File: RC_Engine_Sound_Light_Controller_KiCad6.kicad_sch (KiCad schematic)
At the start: 44 parts, among them J1 RX, J10 RGB, J11 32, J12 CH1, J13 CH2, J14 CH3, J15 ESC, J16 CH4, J17 Brushed Motor output, J2 HeadL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

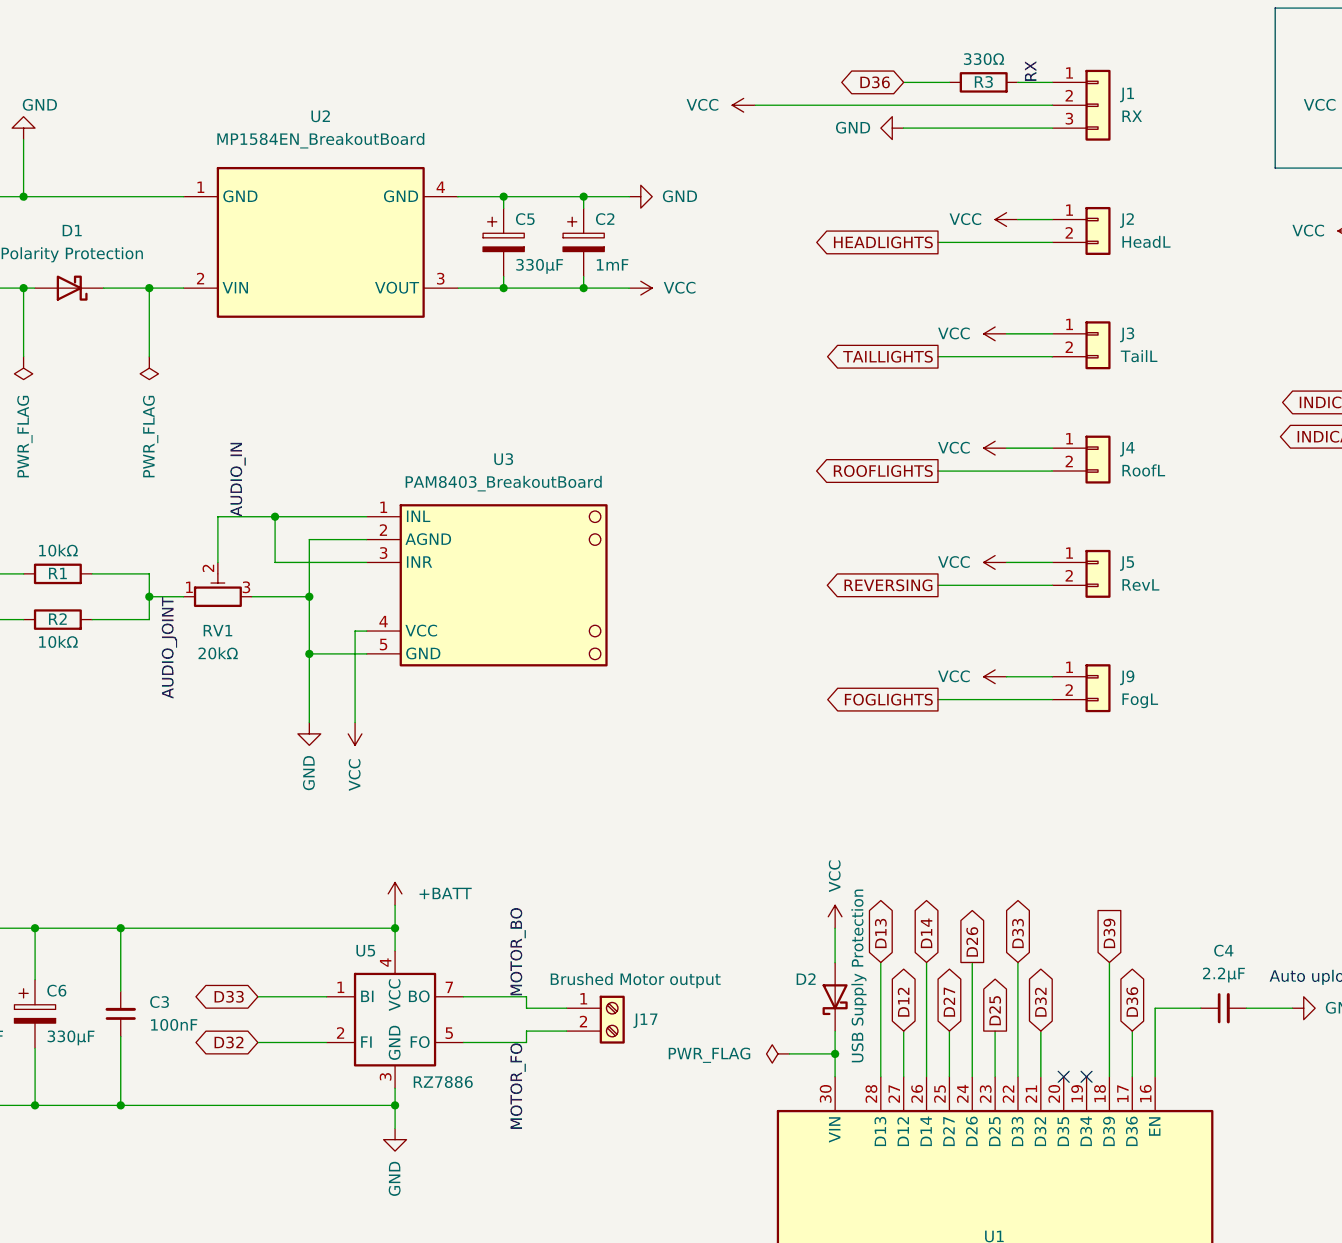
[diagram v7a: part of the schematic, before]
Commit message: Corrected 5V caps silkscreen polarization.
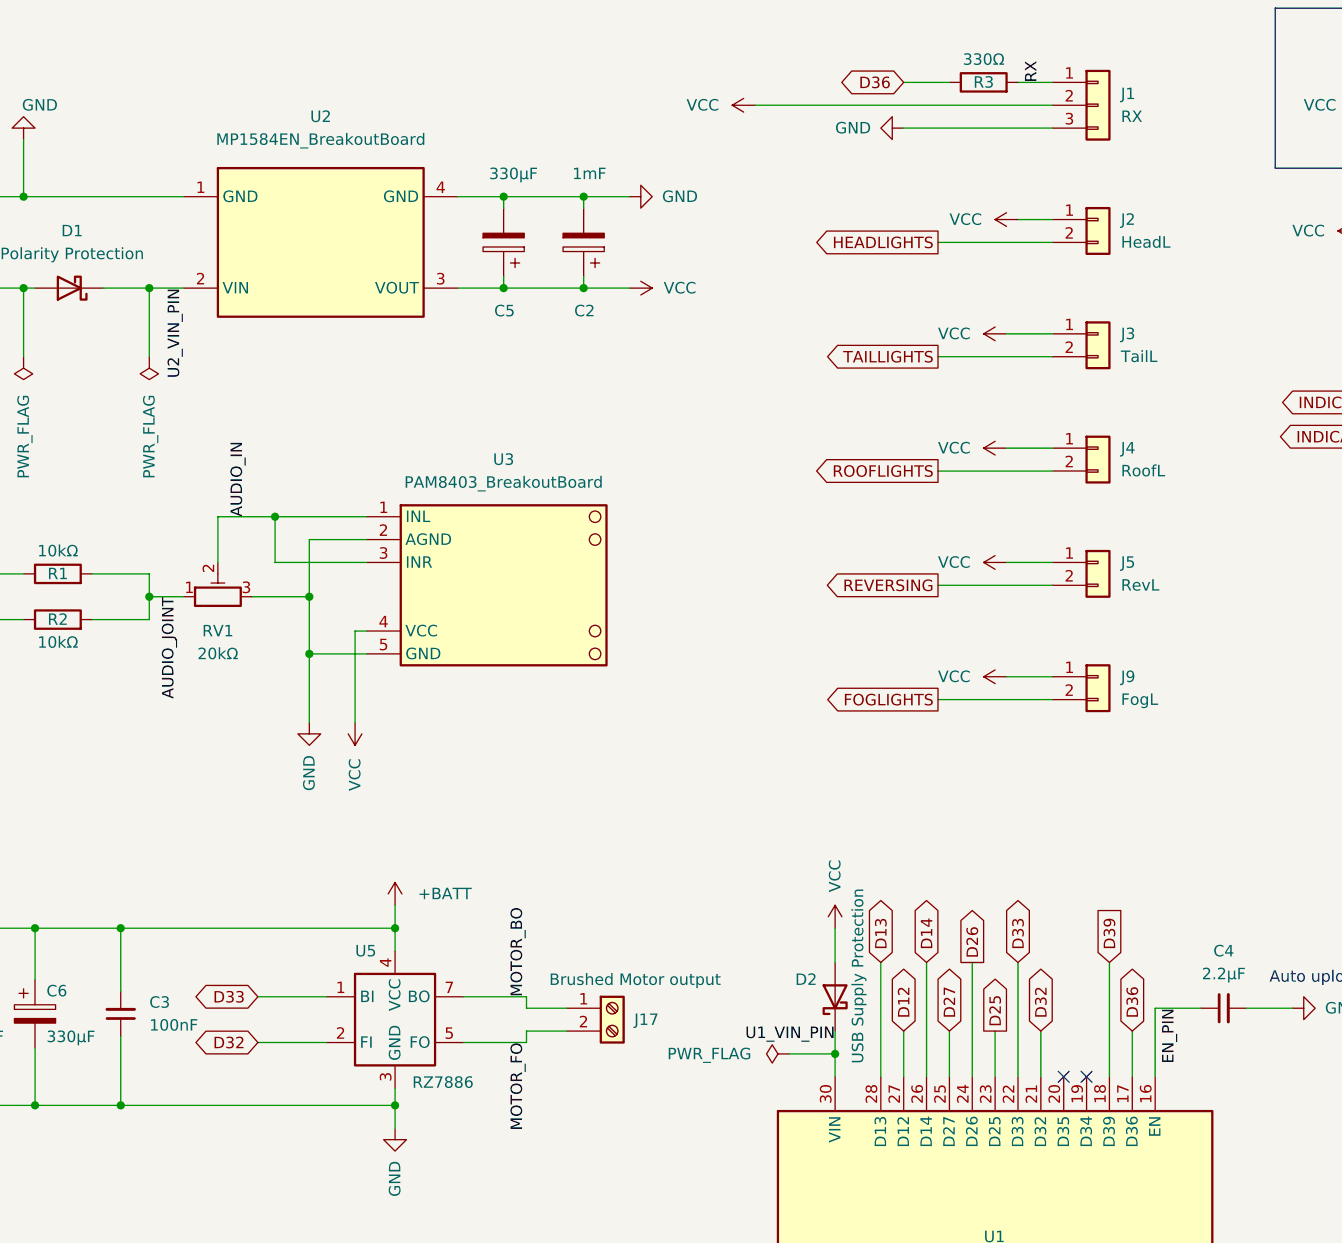
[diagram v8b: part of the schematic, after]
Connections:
- net -BATT: now also C2.2, C5.2; no longer C2.1, C5.1
- net VCC: now also C2.1, C5.1; no longer C2.2, C5.2
- net EN_PIN: now reaches C4.1, U1.16 (EN)
- net U2_VIN_PIN: now reaches D1.1 (K), U2.2 (VIN), U2.6 (VIN)
- net U1_VIN_PIN: now reaches D2.1 (K), U1.30 (VIN)
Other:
- moved on the sheet: C2, C5
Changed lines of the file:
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@@
     (effects (font (size 1.27 1.27)) (justify left bottom))
+  )
+  (label "U1_VIN_PIN" (at 124.46 129.54 180)
+    (effects (font (size 1.27 1.27)) (justify right bottom))
   )
   (label "CH3" (at 266.7 67.31 90)
@@
     (effects (font (size 1.27 1.27)) (justify left bottom))
   )
+  (label "EN_PIN" (at 162.56 125.73 270)
+    (effects (font (size 1.27 1.27)) (justify right bottom))
+  )
   (label "CH4" (at 266.7 82.55 90)
     (effects (font (size 1.27 1.27)) (justify left bottom))
@@
   )
   (label "AUDIO_JOINT" (at 51.435 80.01 270)
+    (effects (font (size 1.27 1.27)) (justify right bottom))
+  )
+  (label "U2_VIN_PIN" (at 52.07 45.72 270)
     (effects (font (size 1.27 1.27)) (justify right bottom))
   )
@@
     (pin "2")
   )
-  (symbol (lib_id "Device:C_Polarized") (at 87.63 40.64 0) (unit 1)
-    (in_bom yes) (on_board yes)
-    (property "Reference" "C5" (id 0) (at 88.9 38.1 0)
-      (effects (font (size 1.27 1.27)) (justify left))
-    )
-    (property "Value" "330µF" (id 1) (at 88.9 43.18 0)
-      (effects (font (size 1.27 1.27)) (justify left))
-    )
-    (property "Footprint" "Capacitor_Tantalum_SMD:CP_EIA-7343-30_AVX-N_Pad2.25x2.55mm_HandSolder" (id 2) (at 88.5952 44.45 0)
+  (symbol (lib_id "Device:C_Polarized") (at 87.63 40.64 180) (unit 1)
+    (in_bom yes) (on_board yes)
+    (property "Reference" "C5" (id 0) (at 88.9 48.26 0)
+      (effects (font (size 1.27 1.27)) (justify left))
+    )
+    (property "Value" "330µF" (id 1) (at 91.44 33.02 0)
+      (effects (font (size 1.27 1.27)) (justify left))
+    )
+    (property "Footprint" "Capacitor_Tantalum_SMD:CP_EIA-7343-30_AVX-N_Pad2.25x2.55mm_HandSolder" (id 2) (at 86.6648 36.83 0)
       (effects (font (size 1.27 1.27)) hide)
     )
@@
     (pin "2")
   )
-  (symbol (lib_id "Device:C_Polarized") (at 96.52 40.64 0) (unit 1)
-    (in_bom yes) (on_board yes)
-    (property "Reference" "C2" (id 0) (at 97.79 38.1 0)
-      (effects (font (size 1.27 1.27)) (justify left))
-    )
-    (property "Value" "1mF" (id 1) (at 97.79 43.18 0)
-      (effects (font (size 1.27 1.27)) (justify left))
-    )
-    (property "Footprint" "Capacitor_THT:CP_Radial_D10.0mm_P2.50mm_P5.00mm" (id 2) (at 97.4852 44.45 0)
-      (effects (font (size 1.27 1.27)) hide)
-    )
+  (symbol (lib_id "Device:C_Polarized") (at 96.52 40.64 180) (unit 1)
+    (in_bom yes) (on_board yes)
+    (property "Reference" "C2" (id 0) (at 97.79 48.26 0)
+      (effects (font (size 1.27 1.27)) (justify left))
+    )
+    (property "Value" "1mF" (id 1) (at 99.06 33.02 0)
+      (effects (font (size 1.27 1.27)) (justify left))
+    )
+    (property "Footprint" "Capacitor_THT:CP_Radial_D10.0mm_P2.50mm_P5.00mm" (id 2) (at 95.5548 36.83 0)
+      (effects (font (size 1.27 1.27)) hide)
+    )
